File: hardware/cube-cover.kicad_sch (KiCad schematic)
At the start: 16 parts

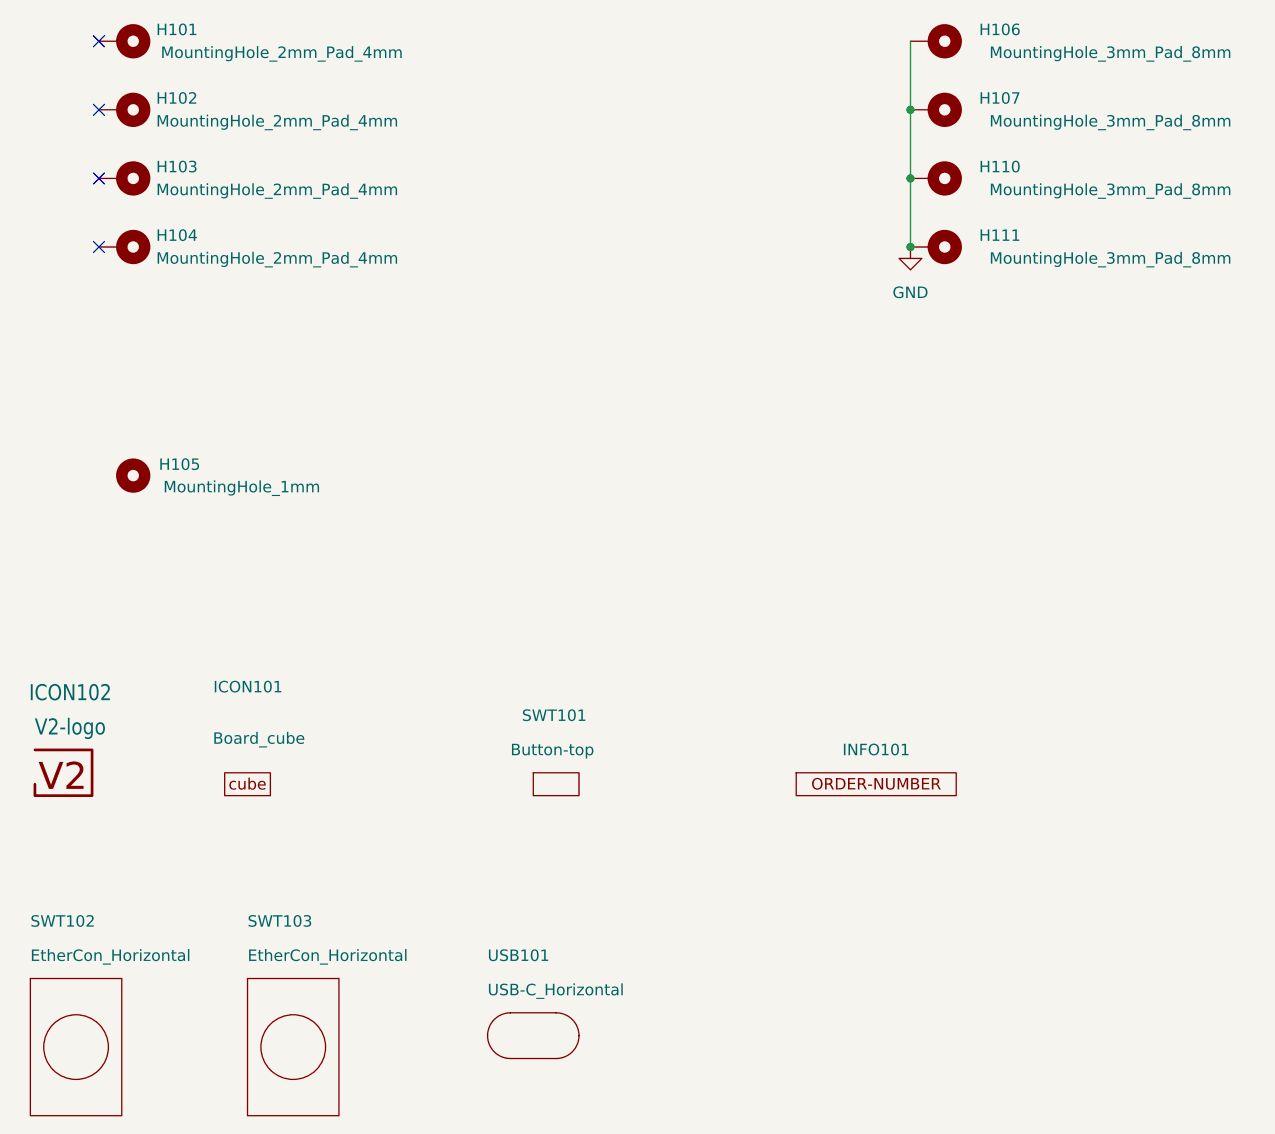
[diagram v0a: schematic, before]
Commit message: Replace Order_Number
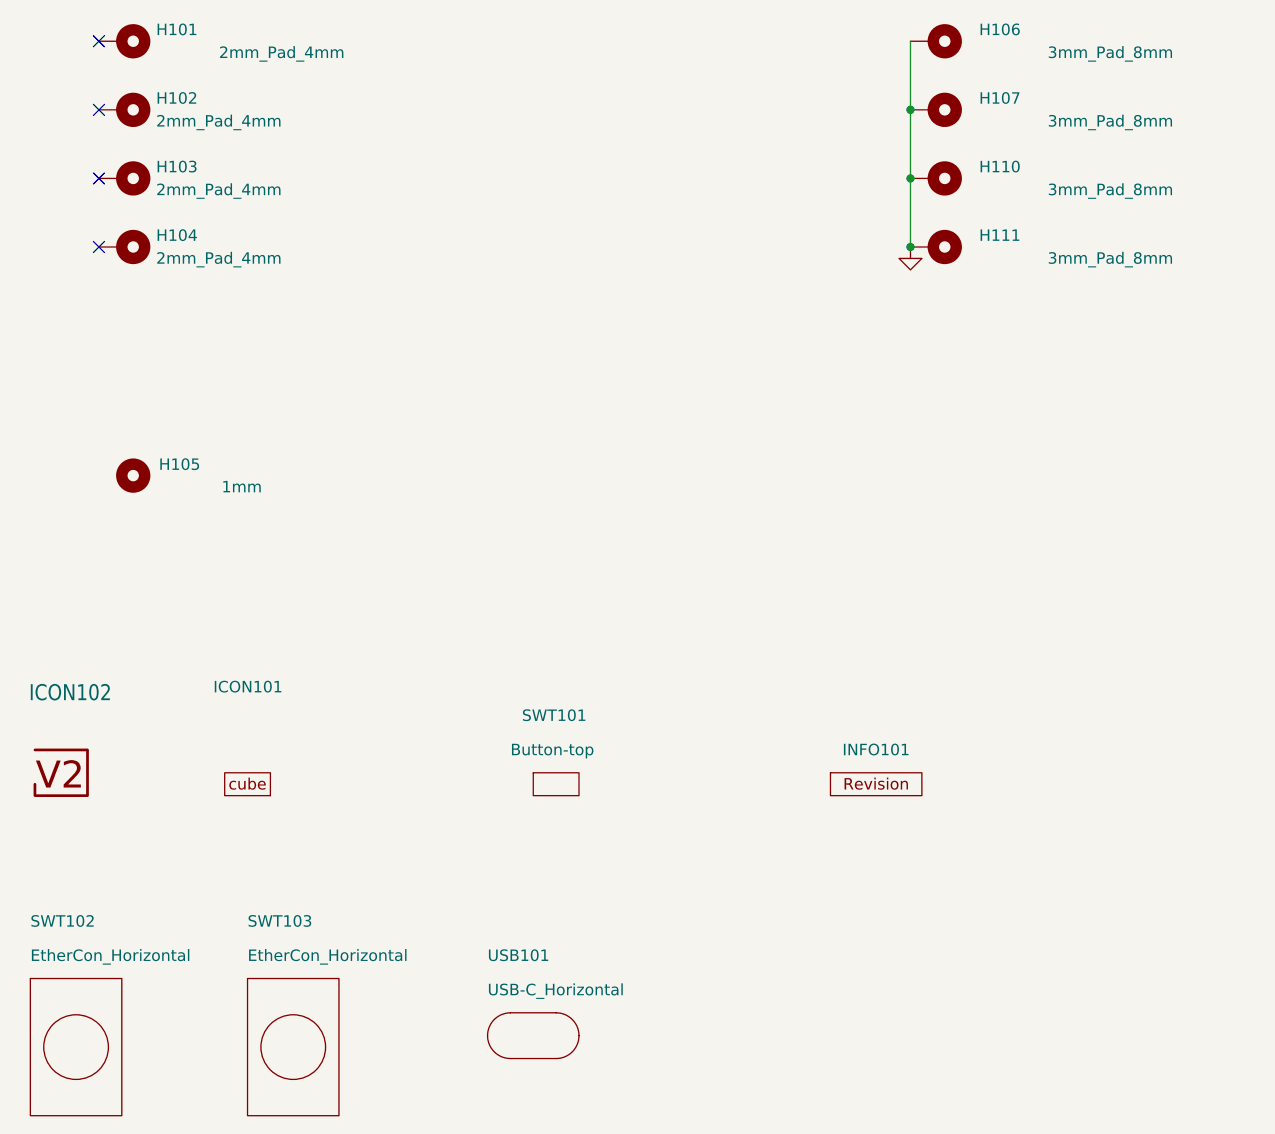
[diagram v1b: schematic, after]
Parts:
- H101, H102, H103, H104: value MountingHole_2mm_Pad_4mm -> 2mm_Pad_4mm
- H105: value MountingHole_1mm -> 1mm
- H106, H107, H110, H111: value MountingHole_3mm_Pad_8mm -> 3mm_Pad_8mm
- INFO101: value ORDER-NUMBER -> ~; footprint V2_Production:Order_Number -> V2_Production:Revision; symbol V2_Production:Order_Number -> V2_Production:Revision
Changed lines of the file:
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@@
 (kicad_sch
-	(version 20231120)
+	(version 20250114)
 	(generator "eeschema")
-	(generator_version "8.0")
+	(generator_version "9.0")
 	(paper "A4")
 	(title_block
 		(title "V2 cube")
-		(date "2023-07-17")
-		(rev "1")
+		(date "2026-02-13")
+		(rev "2023-07-17")
 		(company "Versio Duo")
 		(comment 1 "Cover")
@@
 		(at 102.87 170.18 0)
 		(unit 1)
-		(exclude_from_sim yes)
+		(exclude_from_sim no)
 		(in_bom no)
 		(on_board yes)
@@
 			)
 		)
+		(property "Sim.Enable" "0"
+			(at 102.87 170.18 0)
+			(effects
+				(font
+					(size 1.27 1.27)
+				)
+				(hide yes)
+			)
+		)
 		(instances
 			(project "cube-cover"
@@
 		(at 107.95 66.04 270)
 		(unit 1)
-		(exclude_from_sim yes)
+		(exclude_from_sim no)
 		(in_bom no)
 		(on_board yes)
@@
 			)
 		)
-		(property "Value" "MountingHole_2mm_Pad_4mm"
+		(property "Value" "2mm_Pad_4mm"
 			(at 111.76 67.3099 90)
 			(effects
@@
 			)
 		)
-		(property "Description" ""
+		(property "Description" "Mounting Hole with connection"
 			(at 107.95 66.04 0)
 			(effects
@@
 		(at 153.67 168.91 0)
 		(unit 1)
-		(exclude_from_sim yes)
+		(exclude_from_sim no)
 		(in_bom no)
 		(on_board yes)
@@
 			)
 		)
+		(property "Sim.Enable" "0"
+			(at 153.67 168.91 0)
+			(effects
+				(font
+					(size 1.27 1.27)
+				)
+				(hide yes)
+			)
+		)
 		(instances
 			(project "cube-cover"
@@
 	)
 	(symbol
-		(lib_id "V2_Production:Order_Number")
+		(lib_id "V2_Production:Revision")
 		(at 191.77 140.97 0)
 		(unit 1)
-		(exclude_from_sim yes)
+		(exclude_from_sim no)
 		(in_bom no)
 		(on_board yes)
@@
 			)
 		)
-		(property "Value" "ORDER-NUMBER"
+		(property "Value" "~"
 			(at 191.77 143.51 0)
 			(effects
@@
 			)
 		)
-		(property "Footprint" "V2_Production:Order_Number"
+		(property "Footprint" "V2_Production:Revision"
 			(at 191.77 146.05 0)
 			(effects
@@
 		(at 156.21 140.97 0)
 		(unit 1)
-		(exclude_from_sim yes)
+		(exclude_from_sim no)
 		(in_bom no)
 		(on_board yes)
@@
 			)
 		)
+		(property "Sim.Enable" "0"
+			(at 156.21 140.97 0)
+			(effects
+				(font
+					(size 1.27 1.27)
+				)
+				(hide yes)
+			)
+		)
 		(instances
 			(project "cube-cover"
@@
 		(at 107.95 81.28 270)
 		(unit 1)
-		(exclude_from_sim yes)
+		(exclude_from_sim no)
 		(in_bom no)
 		(on_board yes)
@@
 			)
 		)
-		(property "Value" "MountingHole_2mm_Pad_4mm"
+		(property "Value" "2mm_Pad_4mm"
 			(at 111.76 82.5499 90)
 			(effects
@@
 			)
 		)
-		(property "Description" ""
+		(property "Description" "Mounting Hole with connection"
 			(at 107.95 81.28 0)
 			(effects
@@
 		(at 198.12 58.42 270)
 		(unit 1)
-		(exclude_from_sim yes)
+		(exclude_from_sim no)
 		(in_bom no)
 		(on_board yes)
@@
 			)
 		)
-		(property "Value" "MountingHole_3mm_Pad_8mm"
+		(property "Value" "3mm_Pad_8mm"
 			(at 217.805 59.69 90)
 			(effects
@@
 			)
 		)
-		(property "Description" ""
+		(property "Description" "Mounting Hole with connection"
 			(at 198.12 58.42 0)
 			(effects
@@
 		(at 107.95 58.42 270)
 		(unit 1)
-		(exclude_from_sim yes)
+		(exclude_from_sim no)
 		(in_bom no)
 		(on_board yes)
@@
 			)
 		)
-		(property "Value" "MountingHole_2mm_Pad_4mm"
+		(property "Value" "2mm_Pad_4mm"
 			(at 125.73 59.6899 90)
 			(effects
@@
 			)
 		)
-		(property "Description" ""
+		(property "Description" "Mounting Hole with connection"
 			(at 107.95 58.42 0)
 			(effects
@@
 		(at 198.12 73.66 270)
 		(unit 1)
-		(exclude_from_sim yes)
+		(exclude_from_sim no)
 		(in_bom no)
 		(on_board yes)
@@
 			)
 		)
-		(property "Value" "MountingHole_3mm_Pad_8mm"
+		(property "Value" "3mm_Pad_8mm"
 			(at 217.805 74.93 90)
 			(effects
@@
 			)
 		)
-		(property "Description" ""
+		(property "Description" "Mounting Hole with connection"
 			(at 198.12 73.66 0)
 			(effects
@@
 	)
 	(symbol
-		(lib_id "power:GND")
+		(lib_id "V2_power:GND")
 		(at 195.58 81.28 0)
 		(unit 1)
@@
 					(size 1.27 1.27)
 				)
+				(hide yes)
 			)
 		)
@@
 		(at 198.12 66.04 270)
 		(unit 1)
-		(exclude_from_sim yes)
+		(exclude_from_sim no)
 		(in_bom no)
 		(on_board yes)
@@
 			)
 		)
-		(property "Value" "MountingHole_3mm_Pad_8mm"
+		(property "Value" "3mm_Pad_8mm"
 			(at 217.805 67.31 90)
 			(effects
@@
 			)
 		)
-		(property "Description" ""
+		(property "Description" "Mounting Hole with connection"
 			(at 198.12 66.04 0)
 			(effects
@@
 		(at 198.12 81.28 270)
 		(unit 1)
-		(exclude_from_sim yes)
+		(exclude_from_sim no)
 		(in_bom no)
 		(on_board yes)
@@
 			)
 		)
-		(property "Value" "MountingHole_3mm_Pad_8mm"
+		(property "Value" "3mm_Pad_8mm"
 			(at 217.805 82.55 90)
 			(effects
@@
 			)
 		)
-		(property "Description" ""
+		(property "Description" "Mounting Hole with connection"
 			(at 198.12 81.28 0)
 			(effects
@@
 		(at 127 170.18 0)
 		(unit 1)
-		(exclude_from_sim yes)
+		(exclude_from_sim no)
 		(in_bom no)
 		(on_board yes)
@@
 			)
 		)
+		(property "Sim.Enable" "0"
+			(at 127 170.18 0)
+			(effects
+				(font
+					(size 1.27 1.27)
+				)
+				(hide yes)
+			)
+		)
 		(instances
 			(project "cube-cover"
@@
 		(at 121.92 140.97 0)
 		(unit 1)
-		(exclude_from_sim yes)
+		(exclude_from_sim no)
 		(in_bom no)
 		(on_board yes)
@@
 					(size 1.27 1.27)
 				)
+				(hide yes)
 			)
 		)
@@
 			)
 		)
+		(property "Sim.Enable" "0"
+			(at 121.92 140.97 0)
+			(effects
+				(font
+					(size 1.27 1.27)
+				)
+				(hide yes)
+			)
+		)
 		(instances
 			(project "cube-cover"
@@
 		(at 109.22 106.68 0)
 		(unit 1)
-		(exclude_from_sim yes)
+		(exclude_from_sim no)
 		(in_bom no)
 		(on_board yes)
@@
 			)
 		)
-		(property "Value" "MountingHole_1mm"
+		(property "Value" "1mm"
 			(at 121.285 107.95 0)
 			(effects
@@
 			)
 		)
-		(property "Description" ""
+		(property "Description" "Mounting Hole without connection"
 			(at 109.22 106.68 0)
 			(effects
@@
 		(at 101.6 139.7 0)
 		(unit 1)
-		(exclude_from_sim yes)
+		(exclude_from_sim no)
 		(in_bom no)
 		(on_board yes)
@@
 					(size 1.778 1.5113)
 				)
+				(hide yes)
 			)
 		)
@@
 		(at 107.95 73.66 270)
 		(unit 1)
-		(exclude_from_sim yes)
+		(exclude_from_sim no)
 		(in_bom no)
 		(on_board yes)
@@
 			)
 		)
-		(property "Value" "MountingHole_2mm_Pad_4mm"
+		(property "Value" "2mm_Pad_4mm"
 			(at 111.76 74.9299 90)
 			(effects
@@
 			)
 		)
-		(property "Description" ""
+		(property "Description" "Mounting Hole with connection"
 			(at 107.95 73.66 0)
 			(effects
@@
 		)
 	)
+	(embedded_fonts no)
 )

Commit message: Update Library
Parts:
- INFO101: value ~ -> (none)
- renumbered SWT102 to CON102, SWT103 to CON103
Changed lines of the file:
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@@
 		(on_board yes)
 		(dnp no)
-		(property "Reference" "SWT102"
+		(property "Reference" "CON102"
 			(at 97.79 156.21 0)
 			(effects
@@
 			(project "cube-cover"
 				(path "/6c8448b4-b04d-47e1-934e-e40cbe27a7be"
-					(reference "SWT102")
+					(reference "CON102")
 					(unit 1)
 				)
@@
 			)
 		)
-		(property "Value" "~"
+		(property "Value" ""
 			(at 191.77 143.51 0)
 			(effects
@@
 		)
 		(property "Value" "2mm_Pad_4mm"
-			(at 125.73 59.6899 90)
+			(at 119.38 59.6899 90)
 			(effects
 				(font
@@
 		(dnp no)
 		(fields_autoplaced yes)
-		(property "Reference" "#PWR0101"
+		(property "Reference" "#PWR101"
 			(at 195.58 87.63 0)
 			(effects
@@
 			(project "cube-cover"
 				(path "/6c8448b4-b04d-47e1-934e-e40cbe27a7be"
-					(reference "#PWR0101")
+					(reference "#PWR101")
 					(unit 1)
 				)
@@
 		(on_board yes)
 		(dnp no)
-		(property "Reference" "SWT103"
+		(property "Reference" "CON103"
 			(at 121.92 156.21 0)
 			(effects
@@
 			(project "cube-cover"
 				(path "/6c8448b4-b04d-47e1-934e-e40cbe27a7be"
-					(reference "SWT103")
+					(reference "CON103")
 					(unit 1)
 				)
@@
 		)
 		(property "Value" "1mm"
-			(at 121.285 107.95 0)
-			(effects
-				(font
+			(at 114.681 107.95 0)
+			(effects
+				(font
